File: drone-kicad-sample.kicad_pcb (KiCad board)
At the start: 2 copper layers, 19.5 x 24 mm, 9 parts, among them J1 Screw_Terminal_01x02, J2 Screw_Terminal_01x02

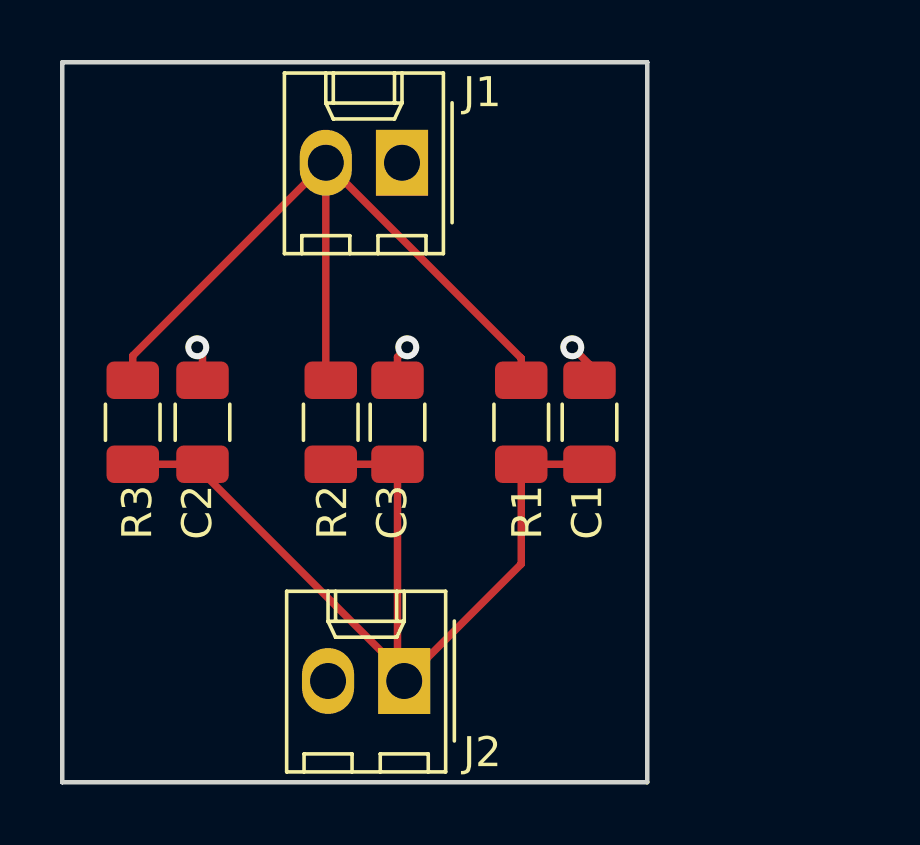
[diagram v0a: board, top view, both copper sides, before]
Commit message: Move componentes
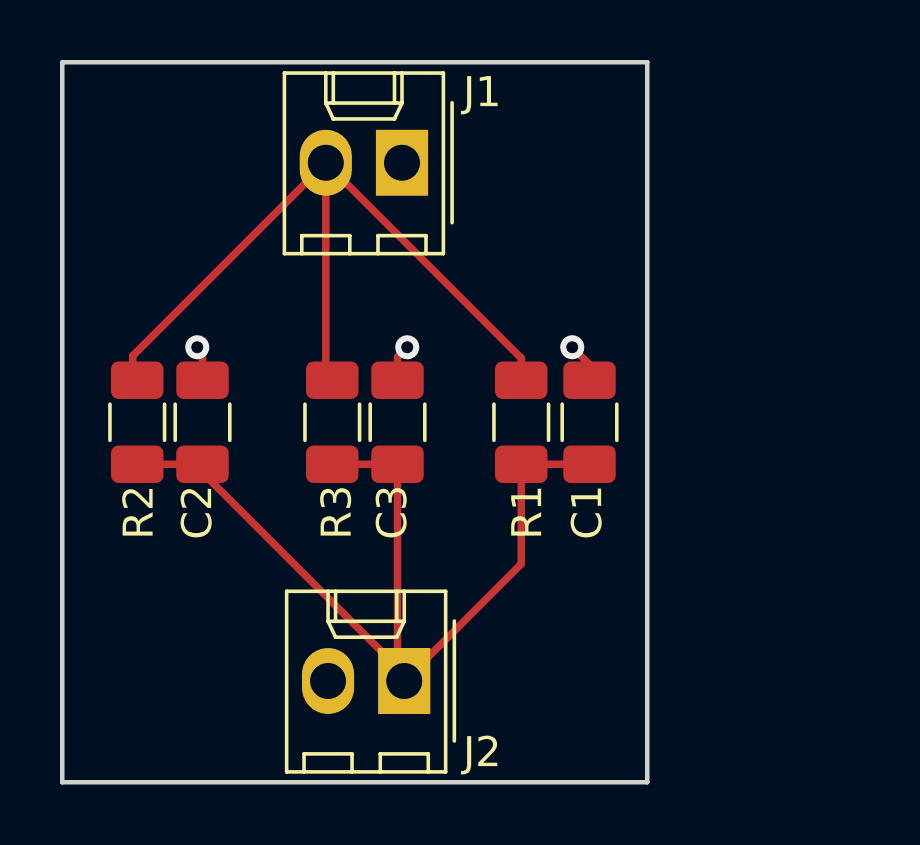
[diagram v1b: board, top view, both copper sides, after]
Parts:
- moved R3 6.65 mm to (144.0, 76.0)
- moved R2 6.45 mm to (137.5, 76.0)
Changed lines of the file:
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@@
   )
   (module Resistor_SMD:R_1206_3216Metric (layer F.Cu)
-    (at 137.35 76 90)
+    (at 144 76 90)
     (descr "Resistor SMD 1206 (3216 Metric), square (rectangular) end terminal, IPC_7351 nominal, (Body size source: http://www.tortai-tech.com/upload/download/2011102023233369053.pdf), generated with kicad-footprint-generator")
     (tags resistor)
@@
   )
   (module Resistor_SMD:R_1206_3216Metric (layer F.Cu)
-    (at 143.95 76 90)
+    (at 137.5 76 90)
     (descr "Resistor SMD 1206 (3216 Metric), square (rectangular) end terminal, IPC_7351 nominal, (Body size source: http://www.tortai-tech.com/upload/download/2011102023233369053.pdf), generated with kicad-footprint-generator")
     (tags resistor)

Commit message: Fix pipeline and board
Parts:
- removed REF**: commit-trace-small, toroid-kicad:commit-trace
- added t1: commit-trace, toroid-kicad:commit-trace, F.Cu at (158.0, 75.5)
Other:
- board size 19.5 x 24 mm -> 26.5 x 24 mm
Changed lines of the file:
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@@
     (add_net "Net-(J1-Pad2)")
+  )
+  (module toroid-kicad:commit-trace (layer F.Cu)
+    (at 158 75.5 90)
+    (fp_text reference t1 (at -5.3 3.5 90) (layer F.SilkS) hide
+      (effects (font (size 1 1) (thickness 0.15)))
+    )
+    (fp_text value commit-trace (at 0.1 -4.4 90) (layer F.Fab) hide
+      (effects (font (size 1 1) (thickness 0.15)))
+    )
+    (fp_text user COMMIT: (at -4 -2 90) (layer F.SilkS)
+      (effects (font (size 1 1) (thickness 0.15) italic))
+    )
+    (fp_text user TAG: (at -5.5 -0.25 90) (layer F.SilkS)
+      (effects (font (size 1 1) (thickness 0.15) italic))
+    )
+    (fp_text user DATE: (at -5 1.5 90) (layer F.SilkS)
+      (effects (font (size 1 1) (thickness 0.15) italic))
+    )
+    (fp_line (start -6.75 -3) (end 6.75 -3) (layer F.SilkS) (width 0.15))
+    (fp_line (start 7.5 -2.25) (end 7.5 1.75) (layer F.SilkS) (width 0.15))
+    (fp_line (start 6.75 2.5) (end -6.75 2.5) (layer F.SilkS) (width 0.15))
+    (fp_line (start -7.5 1.75) (end -7.5 -2.25) (layer F.SilkS) (width 0.15))
+    (fp_arc (start -6.75 -2.25) (end -6.75 -3) (angle -90) (layer F.SilkS) (width 0.15))
+    (fp_arc (start -6.75 1.75) (end -7.5 1.75) (angle -90) (layer F.SilkS) (width 0.15))
+    (fp_arc (start 6.75 1.75) (end 6.75 2.5) (angle -90) (layer F.SilkS) (width 0.15))
+    (fp_arc (start 6.75 -2.25) (end 7.5 -2.25) (angle -90) (layer F.SilkS) (width 0.15))
+    (fp_text user $commit$ (at 3.25 -2 90) (layer F.SilkS)
+      (effects (font (size 0.8 0.8) (thickness 0.2)))
+    )
+    (fp_text user $tag$ (at 3.25 -0.25 90) (layer F.SilkS)
+      (effects (font (size 0.8 0.8) (thickness 0.2)))
+    )
+    (fp_text user $date$ (at 3.25 1.5 90) (layer F.SilkS)
+      (effects (font (size 0.8 0.8) (thickness 0.2)))
+    )
   )
   (module Capacitor_SMD:C_1206_3216Metric (layer F.Cu)
@@
     )
   )
-  (module toroid-kicad:commit-trace (layer B.Cu)
-    (at 145 78.5)
-    (fp_text reference REF** (at -5.3 -3.5) (layer B.SilkS) hide
-      (effects (font (size 1 1) (thickness 0.15)) (justify mirror))
-    )
-    (fp_text value commit-trace-small (at 0.1 4.4) (layer B.Fab) hide
-      (effects (font (size 1 1) (thickness 0.15)) (justify mirror))
-    )
-    (fp_text user $date$ (at 3.25 -1.5) (layer B.SilkS)
-      (effects (font (size 0.8 0.8) (thickness 0.2)) (justify mirror))
-    )
-    (fp_text user $tag$ (at 3.25 0.25) (layer B.SilkS)
-      (effects (font (size 0.8 0.8) (thickness 0.2)) (justify mirror))
-    )
-    (fp_text user $commit$ (at 3.25 2) (layer B.SilkS)
-      (effects (font (size 0.8 0.8) (thickness 0.2)) (justify mirror))
-    )
-    (fp_arc (start 6.75 2.25) (end 7.5 2.25) (angle 90) (layer B.SilkS) (width 0.15))
-    (fp_arc (start 6.75 -1.75) (end 6.75 -2.5) (angle 90) (layer B.SilkS) (width 0.15))
-    (fp_arc (start -6.75 -1.75) (end -7.5 -1.75) (angle 90) (layer B.SilkS) (width 0.15))
-    (fp_arc (start -6.75 2.25) (end -6.75 3) (angle 90) (layer B.SilkS) (width 0.15))
-    (fp_line (start -7.5 -1.75) (end -7.5 2.25) (layer B.SilkS) (width 0.15))
-    (fp_line (start 6.75 -2.5) (end -6.75 -2.5) (layer B.SilkS) (width 0.15))
-    (fp_line (start 7.5 2.25) (end 7.5 -1.75) (layer B.SilkS) (width 0.15))
-    (fp_line (start -6.75 3) (end 6.75 3) (layer B.SilkS) (width 0.15))
-    (fp_text user DATE: (at -5 -1.5) (layer B.SilkS)
-      (effects (font (size 1 1) (thickness 0.15) italic) (justify mirror))
-    )
-    (fp_text user TAG: (at -5.5 0.25) (layer B.SilkS)
-      (effects (font (size 1 1) (thickness 0.15) italic) (justify mirror))
-    )
-    (fp_text user COMMIT: (at -4 2) (layer B.SilkS)
-      (effects (font (size 1 1) (thickness 0.15) italic) (justify mirror))
-    )
-  )
   (gr_line (start 135 88) (end 135 64) (layer Edge.Cuts) (width 0.15))
-  (gr_line (start 154.5 88) (end 135 88) (layer Edge.Cuts) (width 0.15))
-  (gr_line (start 154.5 64) (end 154.5 88) (layer Edge.Cuts) (width 0.15))
-  (gr_line (start 135 64) (end 154.5 64) (layer Edge.Cuts) (width 0.15))
+  (gr_line (start 161.504716 88) (end 135 88) (layer Edge.Cuts) (width 0.15))
+  (gr_line (start 161.5 64) (end 161.5 88) (layer Edge.Cuts) (width 0.15))
+  (gr_line (start 135 64) (end 161.5 64) (layer Edge.Cuts) (width 0.15))
   (segment (start 137.35 77.4) (end 139.675 77.4) (width 0.25) (layer F.Cu) (net 1))
   (segment (start 143.95 77.4) (end 146.175 77.4) (width 0.25) (layer F.Cu) (net 1))
@@
     (polygon
       (pts
-        (xy 135 64) (xy 154.5 64) (xy 154.5 88) (xy 135 88)
+        (xy 135 64) (xy 161.5 64) (xy 161.5 88) (xy 135 88)
       )
     )
@@
     (polygon
       (pts
-        (xy 135 64) (xy 154.5 64) (xy 154.5 88) (xy 135 88)
+        (xy 135 64) (xy 161.5 64) (xy 161.5 88) (xy 135 88)
       )
     )
